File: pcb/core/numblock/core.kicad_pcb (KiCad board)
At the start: 2 copper layers, 79.3 x 78.9 mm, 26 parts, among them J1 Conn_01x11, J2 Conn_01x11, SW1 SW_Push_45deg, SW2 SW_Push_45deg, SW3 SW_Push_45deg, SW4 SW_Push_45deg, SW5 SW_Push_45deg, SW6 SW_Push_45deg, SW7 SW_Push_45deg, SW8 SW_Push_45deg, SW9 SW_Push_45deg, U1 Helios

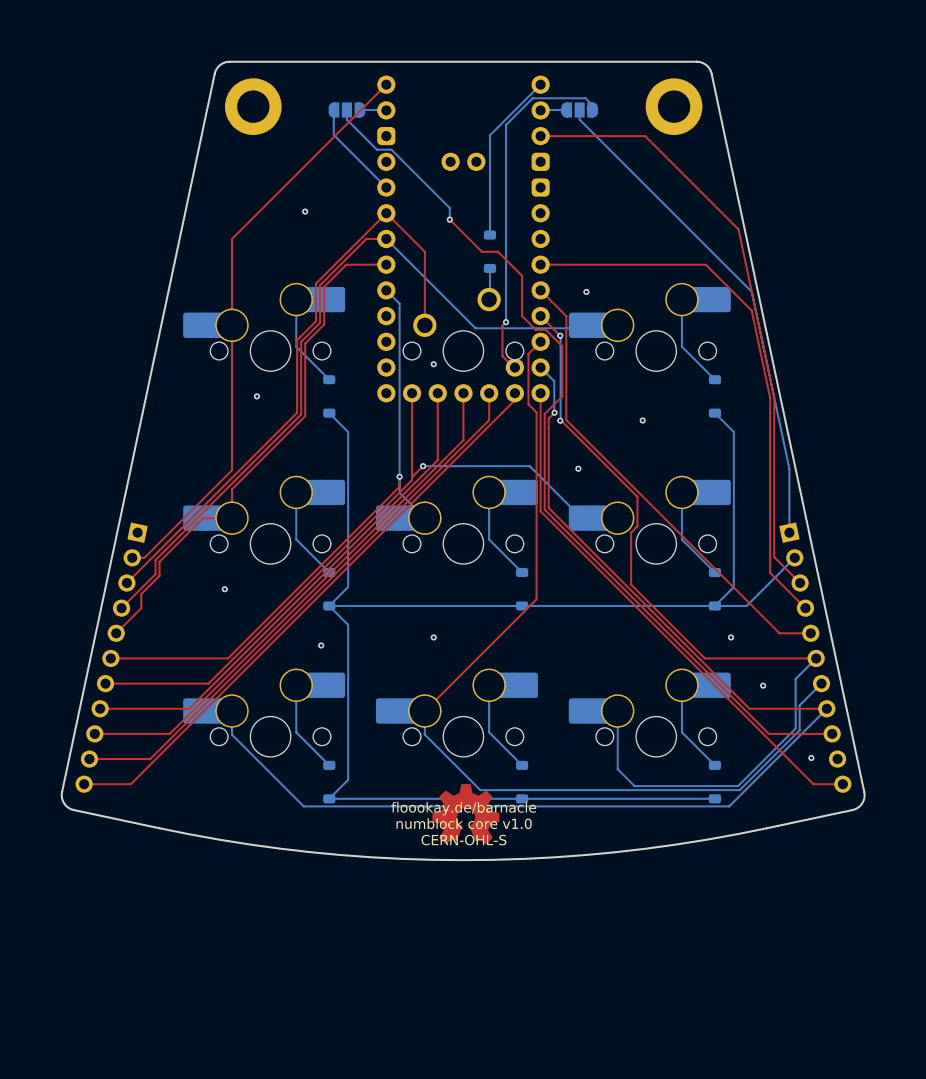
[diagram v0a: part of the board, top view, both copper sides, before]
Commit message: added break off key to the numpad core
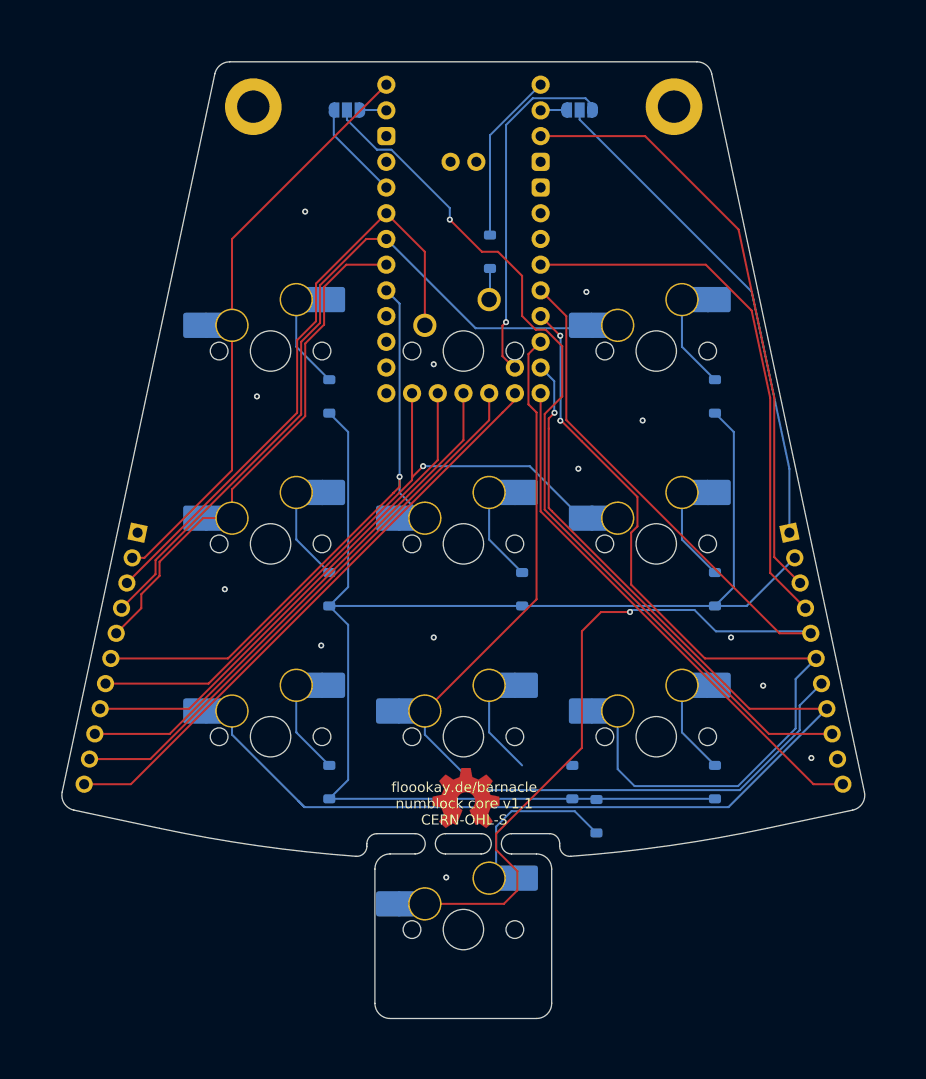
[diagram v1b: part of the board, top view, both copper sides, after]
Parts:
- added D10: D, barnacle:D_SOD-123-minimal, B.Cu at (211.3, 209.0)
- added SW10: SW_Push_45deg, PCM_marbastlib-mx:SW_MX_HS_S_CPG151101S11_1u, B.Cu at (198.2, 220.2)
- moved D8 4.96 mm to (209.0, 205.6)
- moved REF** 1.59 mm to (198.4, 207.2)
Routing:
- net col9: track 46.7 -> 110.8 mm, vias 0 -> 1
- net Net-(D10-A): track 0.00 -> 16.8 mm
- net col6: track 118.4 -> 119.2 mm
- net GND: vias 12 -> 13
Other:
- board size 79.3 x 78.9 mm -> 79.3 x 94.5 mm
- board text added: "floookay.de/barnacle numblock core v1.1 CERN-OHL-S"
- board text removed: "floookay.de/barnacle numblock core v1.0 CERN-OHL-S"
